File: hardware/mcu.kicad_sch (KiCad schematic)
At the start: 36 parts, among them J2 Conn_01x03_Socket, J3 Conn_01x03_Socket, SW1 SW_Push, U1 STM32F405RGT7, X1 8MHz

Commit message: feat(kicad): Updated via  spacing to prevent cutting up the ground plane
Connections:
- net BARO_CS: now also U1.45 (PA12); no longer U1.44 (PA11)
- net BARO_INT: now also U1.44 (PA11); no longer U1.45 (PA12)
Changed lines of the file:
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@@
-		)
-	)
-	(hierarchical_label "BARO_CS"
-		(shape output)
-		(at 167.64 76.2 0)
-		(effects
-			(font
-				(size 1.27 1.27)
-			)
-			(justify left)
 		)
 	)
@@
 		)
 	)
+	(hierarchical_label "BARO_INT"
+		(shape input)
+		(at 167.64 76.2 0)
+		(effects
+			(font
+				(size 1.27 1.27)
+			)
+			(justify left)
+		)
+	)
+	(hierarchical_label "BARO_CS"
+		(shape output)
+		(at 167.64 78.74 0)
+		(effects
+			(font
+				(size 1.27 1.27)
+			)
+			(justify left)
+		)
+	)
 	(hierarchical_label "RADIO_ALT_CS"
 		(shape output)
@@
 		(effects
 			(font
-				(size 1.27 1.27)
-			)
-			(justify left)
-		)
-	)
-	(hierarchical_label "BARO_INT"
-		(shape input)
-		(at 167.64 78.74 0)
-		(effects
-			(font

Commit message: feat(kicad): Updated traces to reduce power plane slotting Finished inital pass of the NRF layout
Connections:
- net RADIO_CS: now also U1.55 (PB3); no longer U1.54 (PD2)
- net RADIO_INT: now also U1.54 (PD2); no longer U1.55 (PB3)
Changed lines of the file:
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@@
+		)
+	)
+	(hierarchical_label "SPI2_MISO"
+		(shape input)
+		(at 124.46 76.2 180)
+		(effects
+			(font
+				(size 1.27 1.27)
+			)
+			(justify right)
+		)
+	)
+	(hierarchical_label "IMU_CS"
+		(shape output)
+		(at 167.64 55.88 0)
+		(effects
+			(font
+				(size 1.27 1.27)
+			)
+			(justify left)
+		)
+	)
+	(hierarchical_label "RADIO_ALT_CE"
+		(shape output)
+		(at 167.64 119.38 0)
+		(effects
+			(font
+				(size 1.27 1.27)
+			)
+			(justify left)
+		)
+	)
+	(hierarchical_label "SPI1_MISO"
+		(shape input)
+		(at 170.18 63.5 0)
+		(effects
+			(font
+				(size 1.27 1.27)
+			)
+			(justify left)
+		)
+	)
+	(hierarchical_label "M2"
+		(shape output)
+		(at 167.64 86.36 0)
+		(effects
+			(font
+				(size 1.27 1.27)
+			)
+			(justify left)
+		)
+	)
+	(hierarchical_label "FLASH_CS"
+		(shape output)
+		(at 167.64 96.52 0)
+		(effects
+			(font
+				(size 1.27 1.27)
+			)
+			(justify left)
+		)
+	)
+	(hierarchical_label "IMU_INT"
+		(shape input)
+		(at 167.64 58.42 0)
+		(effects
+			(font
+				(size 1.27 1.27)
+			)
+			(justify left)
+		)
+	)
+	(hierarchical_label "BARO_INT"
+		(shape input)
+		(at 167.64 76.2 0)
+		(effects
+			(font
+				(size 1.27 1.27)
+			)
+			(justify left)
+		)
+	)
+	(hierarchical_label "BARO_CS"
+		(shape output)
+		(at 167.64 78.74 0)
+		(effects
+			(font
+				(size 1.27 1.27)
+			)
+			(justify left)
+		)
+	)
+	(hierarchical_label "RADIO_ALT_CS"
+		(shape output)
+		(at 170.18 93.98 0)
+		(effects
+			(font
+				(size 1.27 1.27)
+			)
+			(justify left)
+		)
+	)
+	(hierarchical_label "RADIO_CS"
+		(shape output)
+		(at 167.64 99.06 0)
+		(effects
+			(font
+				(size 1.27 1.27)
+			)
+			(justify left)
+		)
+	)
+	(hierarchical_label "UWB_CS"
+		(shape output)
+		(at 121.92 83.82 180)
+		(effects
+			(font
+				(size 1.27 1.27)
+			)
+			(justify right)
+		)
+	)
+	(hierarchical_label "BAT_SENSE"
+		(shape input)
+		(at 167.64 50.8 0)
+		(effects
+			(font
+				(size 1.27 1.27)
+			)
+			(justify left)
+		)
+	)
+	(hierarchical_label "UWB_INT"
+		(shape input)
+		(at 121.92 81.28 180)
+		(effects
+			(font
+				(size 1.27 1.27)
+			)
+			(justify right)
+		)
+	)
+	(hierarchical_label "SPI3_SCK"
+		(shape output)
+		(at 124.46 96.52 180)
+		(effects
+			(font
+				(size 1.27 1.27)
+			)
+			(justify right)
+		)
+	)
+	(hierarchical_label "RADIO_ALT_INT"
+		(shape input)
+		(at 167.64 116.84 0)
+		(effects
+			(font
+				(size 1.27 1.27)
+			)
+			(justify left)
+		)
+	)
+	(hierarchical_label "M4"
+		(shape output)
+		(at 167.64 48.26 0)
+		(effects
+			(font
+				(size 1.27 1.27)
+			)
+			(justify left)
+		)
+	)
+	(hierarchical_label "SPI1_SCK"
+		(shape output)
+		(at 170.18 60.96 0)
+		(effects
+			(font
+				(size 1.27 1.27)
+			)
+			(justify left)
+		)
+	)
+	(hierarchical_label "UWB_RESET"
+		(shape output)
+		(at 168.91 91.44 0)
+		(effects
+			(font
+				(size 1.27 1.27)
+			)
+			(justify left)
+		)
+	)
+	(hierarchical_label "VL53L1X_INT"
+		(shape input)
+		(at 167.64 121.92 0)
+		(effects
+			(font
+				(size 1.27 1.27)
+			)
+			(justify left)
 		)
 	)
 	(hierarchical_label "RADIO_INT"
 		(shape input)
-		(at 167.64 99.06 0)
-		(effects
-			(font
-				(size 1.27 1.27)
-			)
-			(justify left)
-		)
-	)
-	(hierarchical_label "SPI2_MISO"
-		(shape input)
-		(at 124.46 76.2 180)
-		(effects
-			(font
-				(size 1.27 1.27)
-			)
-			(justify right)
-		)
-	)
-	(hierarchical_label "IMU_CS"
-		(shape output)
-		(at 167.64 55.88 0)
-		(effects
-			(font
-				(size 1.27 1.27)
-			)
-			(justify left)
-		)
-	)
-	(hierarchical_label "RADIO_ALT_CE"
-		(shape output)
-		(at 167.64 119.38 0)
-		(effects
-			(font
-				(size 1.27 1.27)
-			)
-			(justify left)
-		)
-	)
-	(hierarchical_label "SPI1_MISO"
-		(shape input)
-		(at 170.18 63.5 0)
-		(effects
-			(font
-				(size 1.27 1.27)
-			)
-			(justify left)
-		)
-	)
-	(hierarchical_label "M2"
-		(shape output)
-		(at 167.64 86.36 0)
-		(effects
-			(font
-				(size 1.27 1.27)
-			)
-			(justify left)
-		)
-	)
-	(hierarchical_label "FLASH_CS"
-		(shape output)
-		(at 167.64 96.52 0)
-		(effects
-			(font
-				(size 1.27 1.27)
-			)
-			(justify left)
-		)
-	)
-	(hierarchical_label "IMU_INT"
-		(shape input)
-		(at 167.64 58.42 0)
-		(effects
-			(font
-				(size 1.27 1.27)
-			)
-			(justify left)
-		)
-	)
-	(hierarchical_label "BARO_INT"
-		(shape input)
-		(at 167.64 76.2 0)
-		(effects
-			(font
-				(size 1.27 1.27)
-			)
-			(justify left)
-		)
-	)
-	(hierarchical_label "BARO_CS"
-		(shape output)
-		(at 167.64 78.74 0)
-		(effects
-			(font
-				(size 1.27 1.27)
-			)
-			(justify left)
-		)
-	)
-	(hierarchical_label "RADIO_ALT_CS"
-		(shape output)
-		(at 170.18 93.98 0)
-		(effects
-			(font
-				(size 1.27 1.27)
-			)
-			(justify left)
-		)
-	)
-	(hierarchical_label "UWB_CS"
-		(shape output)
-		(at 121.92 83.82 180)
-		(effects
-			(font
-				(size 1.27 1.27)
-			)
-			(justify right)
-		)
-	)
-	(hierarchical_label "BAT_SENSE"
-		(shape input)
-		(at 167.64 50.8 0)
-		(effects
-			(font
-				(size 1.27 1.27)
-			)
-			(justify left)
-		)
-	)
-	(hierarchical_label "UWB_INT"
-		(shape input)
-		(at 121.92 81.28 180)
-		(effects
-			(font
-				(size 1.27 1.27)
-			)
-			(justify right)
-		)
-	)
-	(hierarchical_label "SPI3_SCK"
-		(shape output)
-		(at 124.46 96.52 180)
-		(effects
-			(font
-				(size 1.27 1.27)
-			)
-			(justify right)
-		)
-	)
-	(hierarchical_label "RADIO_ALT_INT"
-		(shape input)
-		(at 167.64 116.84 0)
-		(effects
-			(font
-				(size 1.27 1.27)
-			)
-			(justify left)
-		)
-	)
-	(hierarchical_label "M4"
-		(shape output)
-		(at 167.64 48.26 0)
-		(effects
-			(font
-				(size 1.27 1.27)
-			)
-			(justify left)
-		)
-	)
-	(hierarchical_label "SPI1_SCK"
-		(shape output)
-		(at 170.18 60.96 0)
-		(effects
-			(font
-				(size 1.27 1.27)
-			)
-			(justify left)
-		)
-	)
-	(hierarchical_label "UWB_RESET"
-		(shape output)
-		(at 168.91 91.44 0)
-		(effects
-			(font
-				(size 1.27 1.27)
-			)
-			(justify left)
-		)
-	)
-	(hierarchical_label "VL53L1X_INT"
-		(shape input)
-		(at 167.64 121.92 0)
-		(effects
-			(font
-				(size 1.27 1.27)
-			)
-			(justify left)
-		)
-	)
-	(hierarchical_label "RADIO_CS"
-		(shape output)
 		(at 127 66.04 180)
 		(effects

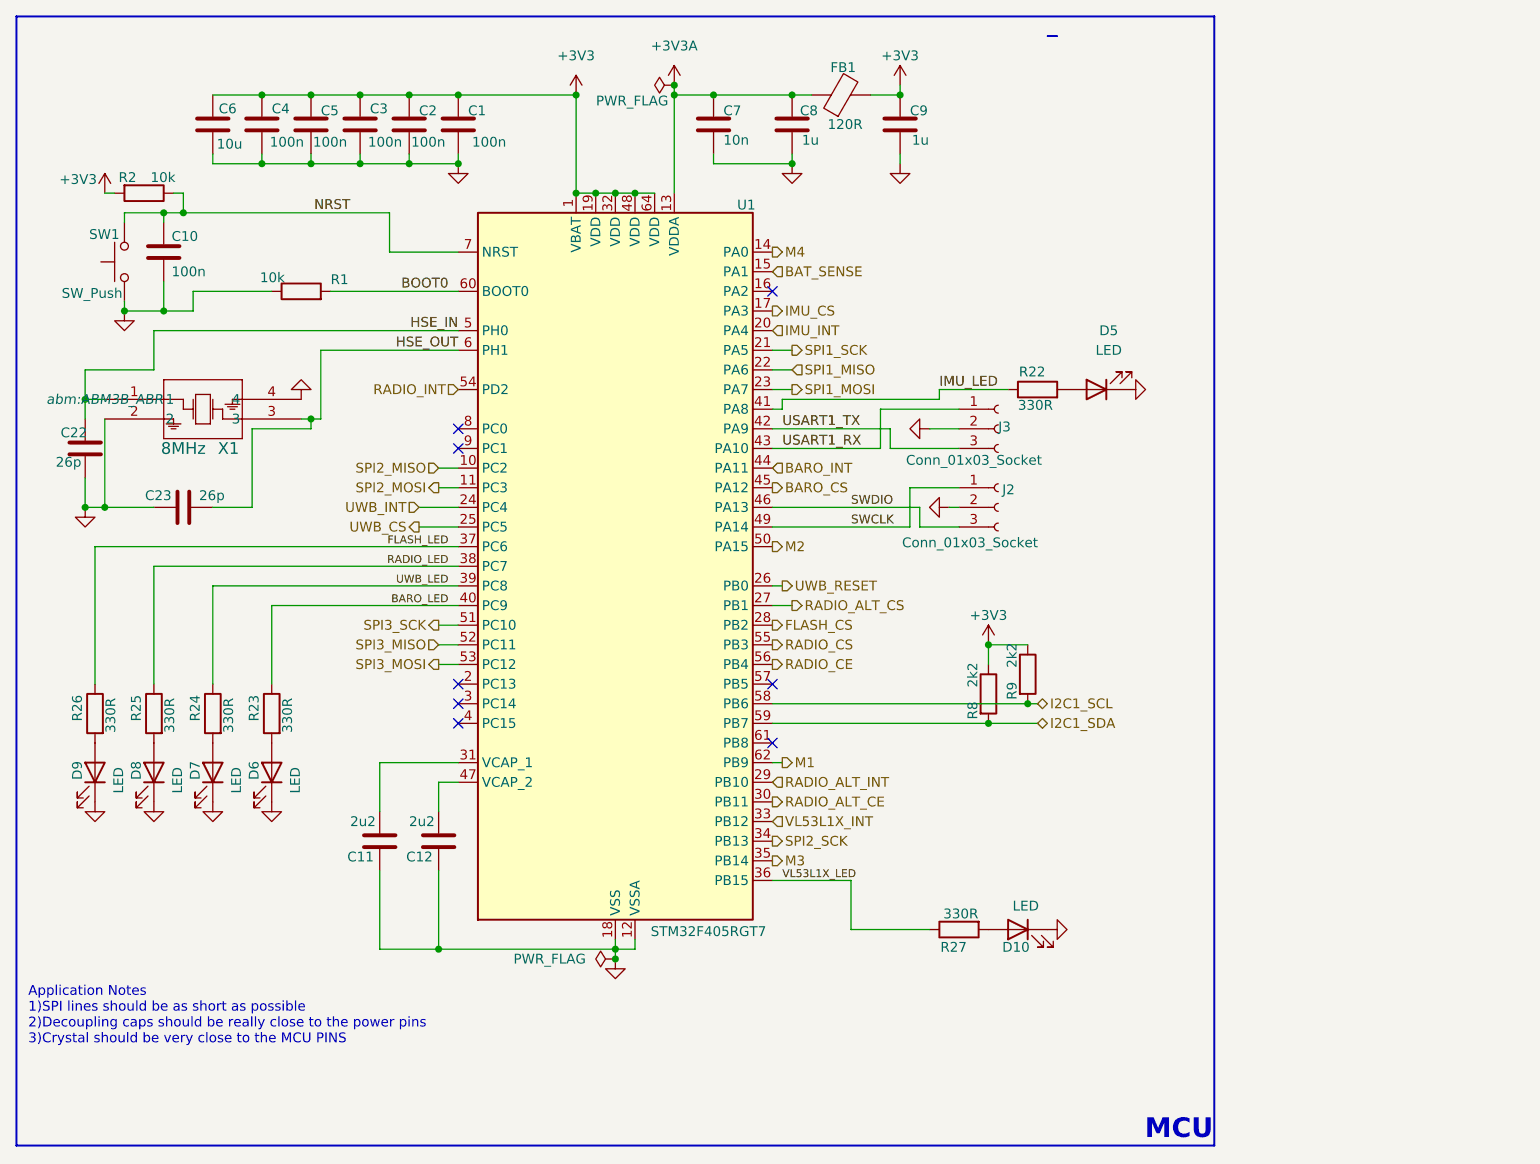
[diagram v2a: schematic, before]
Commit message: feat(kicad): Routing complete, assigning jlc components to each footprint
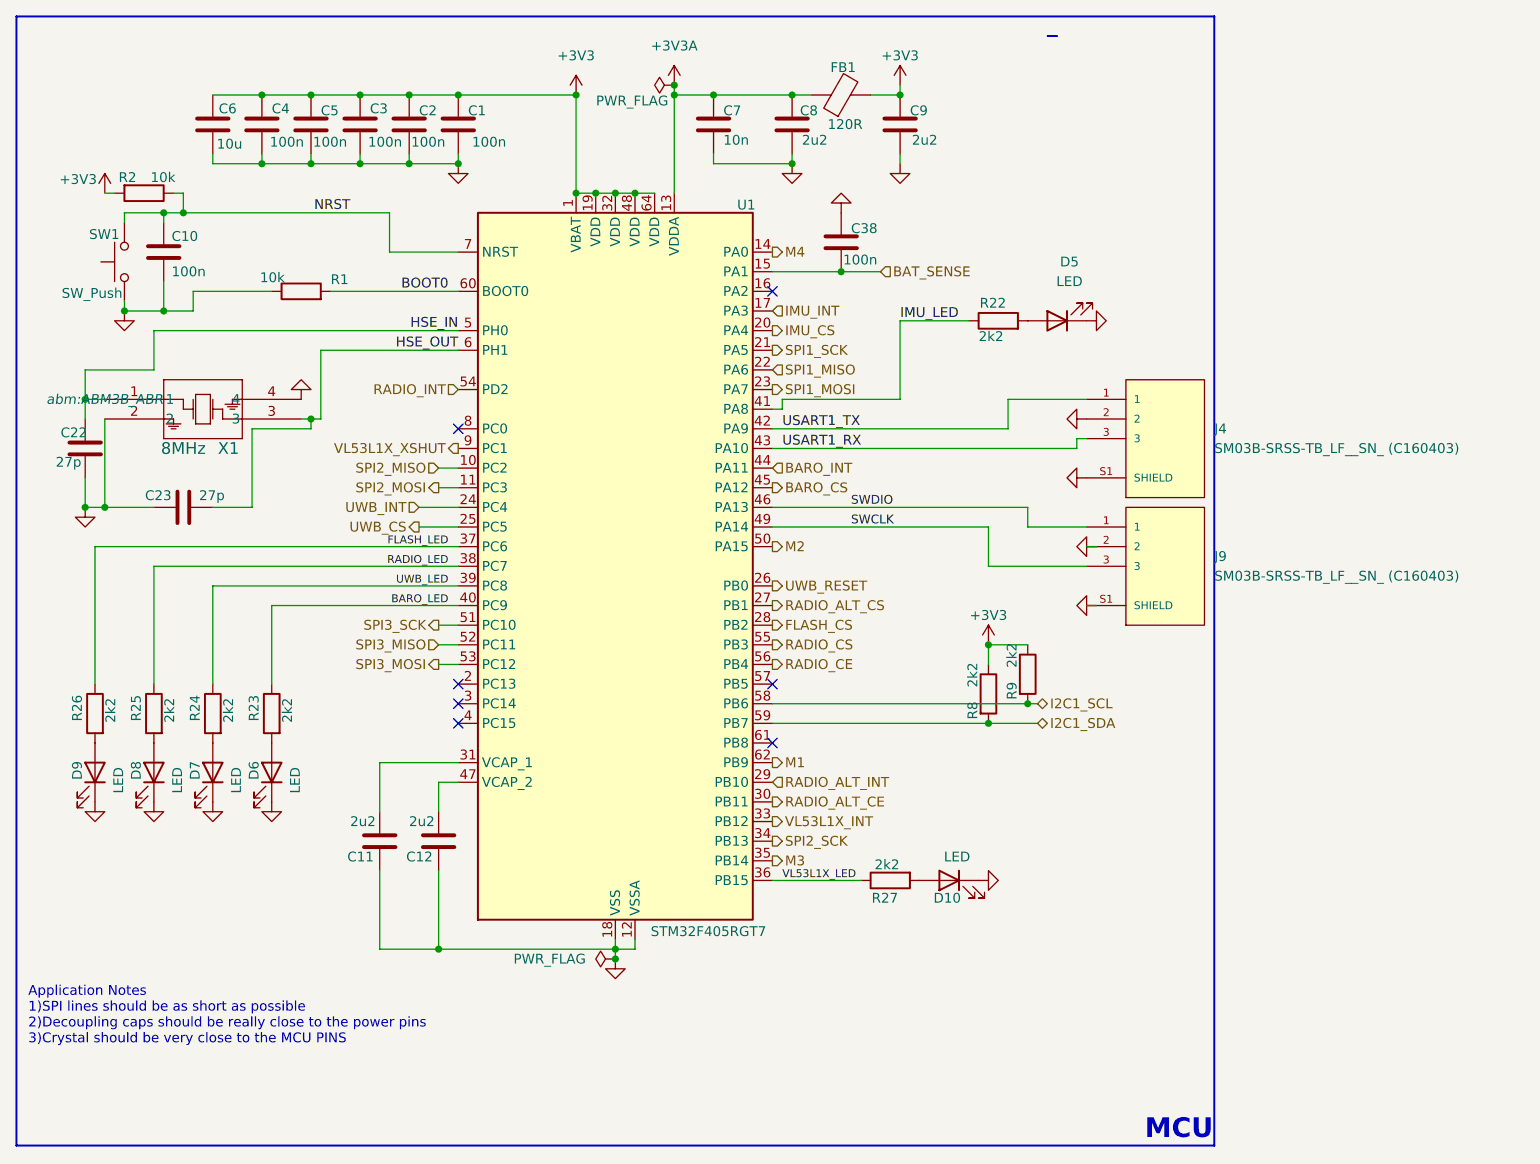
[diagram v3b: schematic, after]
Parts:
- removed J2, J3: Conn_01x03_Socket, Connector_PinHeader_1.00mm:PinHeader_1x03_P1.00mm_Horizontal, symbol Connector:Conn_01x03_Socket
- added C38: 100n, Capacitor_SMD:C_0402_1005Metric, symbol Device:C
- added J4, J9: SM03B-SRSS-TB_LF__SN_ (C160403), header:JST_SM03B-SRSS-TB_LF__SN_, symbol SM03B-SRSS-TB_LF__SN_:SM03B-SRSS-TB_LF__SN_
- C1, C10, C2, C3, C4, C5: LCSC (none) -> C1525
- C22, C23: value 26p -> 27p
- C6: LCSC (none) -> C19702
- C8, C9: value 1u -> 2u2
- D10, D5, D6, D7, D8, D9: LCSC (none) -> C2286
- R1, R2: LCSC (none) -> C25744
- R22, R23, R24, R25, R26, R27: value 330R -> 2k2; LCSC (none) -> C25879
- R8, R9: LCSC (none) -> C25879
- SW1: LCSC (none) -> C720477
- U1: LCSC (none) -> C1337199
- X1: LCSC (none) -> C83312
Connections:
- net BAT_SENSE: now also C38.2
- net GND: now also C38.1, J4.2, J4.S1 (SHIELD), J4.S2 (SHIELD), J9.2, J9.S1 (SHIELD), J9.S2 (SHIELD)
- net IMU_CS: now also U1.20 (PA4); no longer U1.17 (PA3)
- net IMU_INT: now also U1.17 (PA3); no longer U1.20 (PA4)
- net SWCLK: now also J9.3
- net SWDIO: now also J9.1
- net USART1_RX: now also J4.3
- net USART1_TX: now also J4.1
- net VL53L1X_XSHUT: now reaches U1.9 (PC1)
- no-connect marks 8 -> 7
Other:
- moved on the sheet: D10, D5, R22, R27

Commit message: feat(kicad): Cleaned up routing and picked LCSC parts for several components
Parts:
- C11, C12, C8, C9: LCSC (none) -> C12530
- C22, C23: LCSC (none) -> C1557
- C7: LCSC (none) -> C15195
- FB1: LCSC (none) -> C14709
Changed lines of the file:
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@@
 			)
 		)
-		(property "LCSC" ""
+		(property "LCSC" "C12530"
 			(at 124.46 124.46 0)
 			(hide yes)
@@
 			)
 		)
-		(property "LCSC" ""
+		(property "LCSC" "C14709"
 			(at 176.53 27.94 90)
 			(hide yes)
@@
 			)
 		)
-		(property "LCSC" ""
+		(property "LCSC" "C12530"
 			(at 170.18 31.75 0)
 			(hide yes)
@@
 			)
 		)
-		(property "LCSC" ""
+		(property "LCSC" "C15195"
 			(at 160.02 31.75 0)
 			(hide yes)
@@
 			)
 		)
-		(property "LCSC" ""
+		(property "LCSC" "C12530"
 			(at 184.15 31.75 0)
 			(hide yes)
@@
 			)
 		)
-		(property "LCSC" ""
+		(property "LCSC" "C1557"
 			(at 91.44 81.28 90)
 			(hide yes)
@@
 			)
 		)
-		(property "LCSC" ""
+		(property "LCSC" "C12530"
 			(at 116.84 124.46 0)
 			(hide yes)
@@
 			)
 		)
-		(property "LCSC" ""
+		(property "LCSC" "C1557"
 			(at 78.74 73.66 0)
 			(hide yes)
